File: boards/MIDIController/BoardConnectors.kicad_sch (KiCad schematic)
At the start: 16 parts, among them J2 MIDICon, J3 IO_Boards

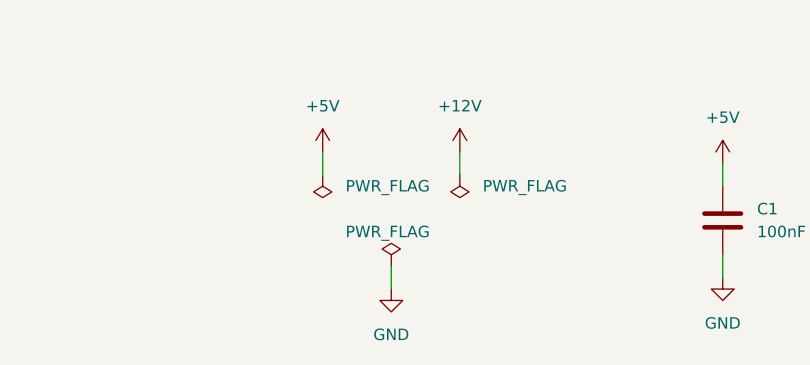
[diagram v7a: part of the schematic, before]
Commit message: Updated design rules to 0.32mm template and exported Gerber files
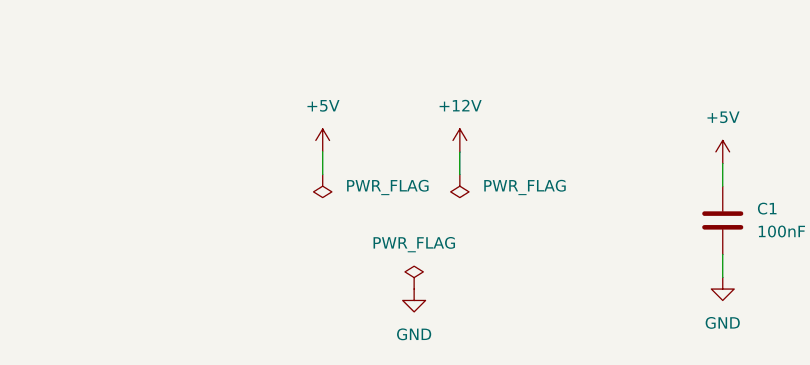
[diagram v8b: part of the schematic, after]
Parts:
- C2: footprint Capacitor_THT:CP_Radial_D7.5mm_P2.50mm -> Capacitor_THT:CP_Radial_D5.0mm_P2.00mm
- C4, C5, C6, C7, C8, C9: footprint Capacitor_THT:C_Disc_D4.3mm_W1.9mm_P5.00mm -> Capacitor_THT:C_Disc_D3.8mm_W2.6mm_P2.50mm
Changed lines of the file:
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@@
 	(wire
 		(pts
-			(xy 110.49 152.4) (xy 110.49 154.94)
-		)
-		(stroke
-			(width 0)
-			(type default)
-		)
-	)
-	(wire
-		(pts
 			(xy 78.74 101.6) (xy 78.74 59.69)
 		)
@@
 			)
 		)
-		(property "Footprint" "Capacitor_THT:C_Disc_D4.3mm_W1.9mm_P5.00mm"
+		(property "Footprint" "Capacitor_THT:C_Disc_D3.8mm_W2.6mm_P2.50mm"
 			(at 57.4548 118.11 0)
 			(effects
@@
 	)
 	(symbol
+		(lib_id "power:GND")
+		(at 113.03 154.94 0)
+		(unit 1)
+		(exclude_from_sim no)
+		(in_bom yes)
+		(on_board yes)
+		(dnp no)
+		(fields_autoplaced yes)
+		(property "Reference" "#PWR09"
+			(at 113.03 161.29 0)
+			(effects
+				(font
+					(size 1.27 1.27)
+				)
+				(hide yes)
+			)
+		)
+		(property "Value" "GND"
+			(at 113.03 160.02 0)
+			(effects
+				(font
+					(size 1.27 1.27)
+				)
+			)
+		)
+		(property "Footprint" ""
+			(at 113.03 154.94 0)
+			(effects
+				(font
+					(size 1.27 1.27)
+				)
+				(hide yes)
+			)
+		)
+		(property "Datasheet" ""
+			(at 113.03 154.94 0)
+			(effects
+				(font
+					(size 1.27 1.27)
+				)
+				(hide yes)
+			)
+		)
+		(property "Description" "Power symbol creates a global label with name \"GND\" , ground"
+			(at 113.03 154.94 0)
+			(effects
+				(font
+					(size 1.27 1.27)
+				)
+				(hide yes)
+			)
+		)
+		(pin "1"
+		)
+		(instances
+			(project "MIDIController"
+				(path "/92e30726-a111-410e-a189-3ef5a23983ec/5462fee6-2428-4e3a-a87e-5f06517bb085"
+					(reference "#PWR09")
+					(unit 1)
+				)
+			)
+		)
+	)
+	(symbol
 		(lib_id "Device:C_Polarized")
 		(at 166.37 147.32 0)
@@
 			)
 		)
-		(property "Footprint" "Capacitor_THT:CP_Radial_D7.5mm_P2.50mm"
+		(property "Footprint" "Capacitor_THT:CP_Radial_D5.0mm_P2.00mm"
 			(at 167.3352 151.13 0)
 			(effects
@@
 			)
 		)
-		(property "Footprint" "Capacitor_THT:C_Disc_D4.3mm_W1.9mm_P5.00mm"
+		(property "Footprint" "Capacitor_THT:C_Disc_D3.8mm_W2.6mm_P2.50mm"
 			(at 57.4548 52.07 0)
 			(effects
@@
 			)
 		)
-		(property "Footprint" "Capacitor_THT:C_Disc_D4.3mm_W1.9mm_P5.00mm"
+		(property "Footprint" "Capacitor_THT:C_Disc_D3.8mm_W2.6mm_P2.50mm"
 			(at 57.4548 101.6 0)
 			(effects
@@
 	)
 	(symbol
-		(lib_id "Device:R")
-		(at 66.04 76.2 90)
-		(mirror x)
-		(unit 1)
-		(exclude_from_sim no)
-		(in_bom yes)
-		(on_board yes)
-		(dnp no)
-		(property "Reference" "R5"
-			(at 66.04 79.248 90)
-			(effects
-				(font
-					(size 1.27 1.27)
-				)
-			)
-		)
-		(property "Value" "100"
-			(at 66.04 81.788 90)
-			(effects
-				(font
-					(size 1.27 1.27)
-				)
-			)
-		)
-		(property "Footprint" "Resistor_THT:R_Axial_DIN0207_L6.3mm_D2.5mm_P10.16mm_Horizontal"
-			(at 66.04 74.422 90)
-			(effects
-				(font
-					(size 1.27 1.27)
-				)
-				(hide yes)
-			)
-		)
-		(property "Datasheet" "~"
-			(at 66.04 76.2 0)
-			(effects
-				(font
-					(size 1.27 1.27)
-				)
-				(hide yes)
-			)
-		)
-		(property "Description" "Resistor"
-			(at 66.04 76.2 0)
-			(effects
-				(font
-					(size 1.27 1.27)
-				)
-				(hide yes)
-			)
-		)
-		(pin "1"
-		)
-		(pin "2"
-		)
-		(instances
-			(project "MIDIController"
-				(path "/92e30726-a111-410e-a189-3ef5a23983ec/5462fee6-2428-4e3a-a87e-5f06517bb085"
-					(reference "R5")
-					(unit 1)
-				)
-			)
-		)
-	)
-	(symbol
 		(lib_id "power:PWR_FLAG")
-		(at 110.49 152.4 0)
+		(at 113.03 154.94 0)
 		(unit 1)
 		(exclude_from_sim no)
@@
 		(on_board yes)
 		(dnp no)
-		(property "Reference" "#FLG02"
-			(at 110.49 150.495 0)
+		(fields_autoplaced yes)
+		(property "Reference" "#FLG07"
+			(at 113.03 153.035 0)
 			(effects
 				(font
@@
 		)
 		(property "Value" "PWR_FLAG"
-			(at 105.41 148.59 0)
+			(at 113.03 149.86 0)
 			(effects
 				(font
 					(size 1.27 1.27)
 				)
-				(justify left)
 			)
 		)
 		(property "Footprint" ""
-			(at 110.49 152.4 0)
+			(at 113.03 154.94 0)
 			(effects
 				(font
@@
 		)
 		(property "Datasheet" "~"
-			(at 110.49 152.4 0)
+			(at 113.03 154.94 0)
 			(effects
 				(font
@@
 		)
 		(property "Description" "Special symbol for telling ERC where power comes from"
-			(at 110.49 152.4 0)
+			(at 113.03 154.94 0)
 			(effects
 				(font
@@
 			(project "MIDIController"
 				(path "/92e30726-a111-410e-a189-3ef5a23983ec/5462fee6-2428-4e3a-a87e-5f06517bb085"
-					(reference "#FLG02")
+					(reference "#FLG07")
 					(unit 1)
 				)
@@
 	)
 	(symbol
-		(lib_id "power:GND")
-		(at 110.49 154.94 0)
+		(lib_id "Device:R")
+		(at 66.04 76.2 90)
+		(mirror x)
 		(unit 1)
 		(exclude_from_sim no)
@@
 		(on_board yes)
 		(dnp no)
-		(fields_autoplaced yes)
-		(property "Reference" "#PWR09"
-			(at 110.49 161.29 0)
+		(property "Reference" "R5"
+			(at 66.04 79.248 90)
 			(effects
 				(font
 					(size 1.27 1.27)
 				)
-				(hide yes)
 			)
 		)
-		(property "Value" "GND"
-			(at 110.49 160.02 0)
+		(property "Value" "100"
+			(at 66.04 81.788 90)
 			(effects
 				(font
@@
 			)
 		)
-		(property "Footprint" ""
-			(at 110.49 154.94 0)
+		(property "Footprint" "Resistor_THT:R_Axial_DIN0207_L6.3mm_D2.5mm_P10.16mm_Horizontal"
+			(at 66.04 74.422 90)
 			(effects
 				(font
@@
 			)
 		)
-		(property "Datasheet" ""
-			(at 110.49 154.94 0)
+		(property "Datasheet" "~"
+			(at 66.04 76.2 0)
 			(effects
 				(font
@@
 			)
 		)
-		(property "Description" "Power symbol creates a global label with name \"GND\" , ground"
-			(at 110.49 154.94 0)
+		(property "Description" "Resistor"
+			(at 66.04 76.2 0)
 			(effects
 				(font
@@
 		(pin "1"
 		)
+		(pin "2"
+		)
 		(instances
 			(project "MIDIController"
 				(path "/92e30726-a111-410e-a189-3ef5a23983ec/5462fee6-2428-4e3a-a87e-5f06517bb085"
-					(reference "#PWR09")
+					(reference "R5")
 					(unit 1)
 				)
@@
 			)
 		)
-		(property "Footprint" "Capacitor_THT:C_Disc_D4.3mm_W1.9mm_P5.00mm"
+		(property "Footprint" "Capacitor_THT:C_Disc_D3.8mm_W2.6mm_P2.50mm"
 			(at 57.4548 68.58 0)
 			(effects
@@
 			)
 		)
-		(property "Footprint" "Capacitor_THT:C_Disc_D4.3mm_W1.9mm_P5.00mm"
+		(property "Footprint" "Capacitor_THT:C_Disc_D3.8mm_W2.6mm_P2.50mm"
 			(at 57.4548 35.56 0)
 			(effects
@@
 			)
 		)
-		(property "Footprint" "Capacitor_THT:C_Disc_D4.3mm_W1.9mm_P5.00mm"
+		(property "Footprint" "Capacitor_THT:C_Disc_D3.8mm_W2.6mm_P2.50mm"
 			(at 57.4548 85.09 0)
 			(effects
